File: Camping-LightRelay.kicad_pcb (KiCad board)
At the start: 2 copper layers, 58 x 63 mm, 91 parts, among them CN1 U262-061N-4BVC11, CN101 XHP-2, CN2 907-152A1022D10200, CN3 907-152A1022D10200, CN4 B2B-XH-A, Q1 FDV301N, Q2 BC817, Q3 IRF7404, Q4 BSS138, U1 USBLC6-2SC6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

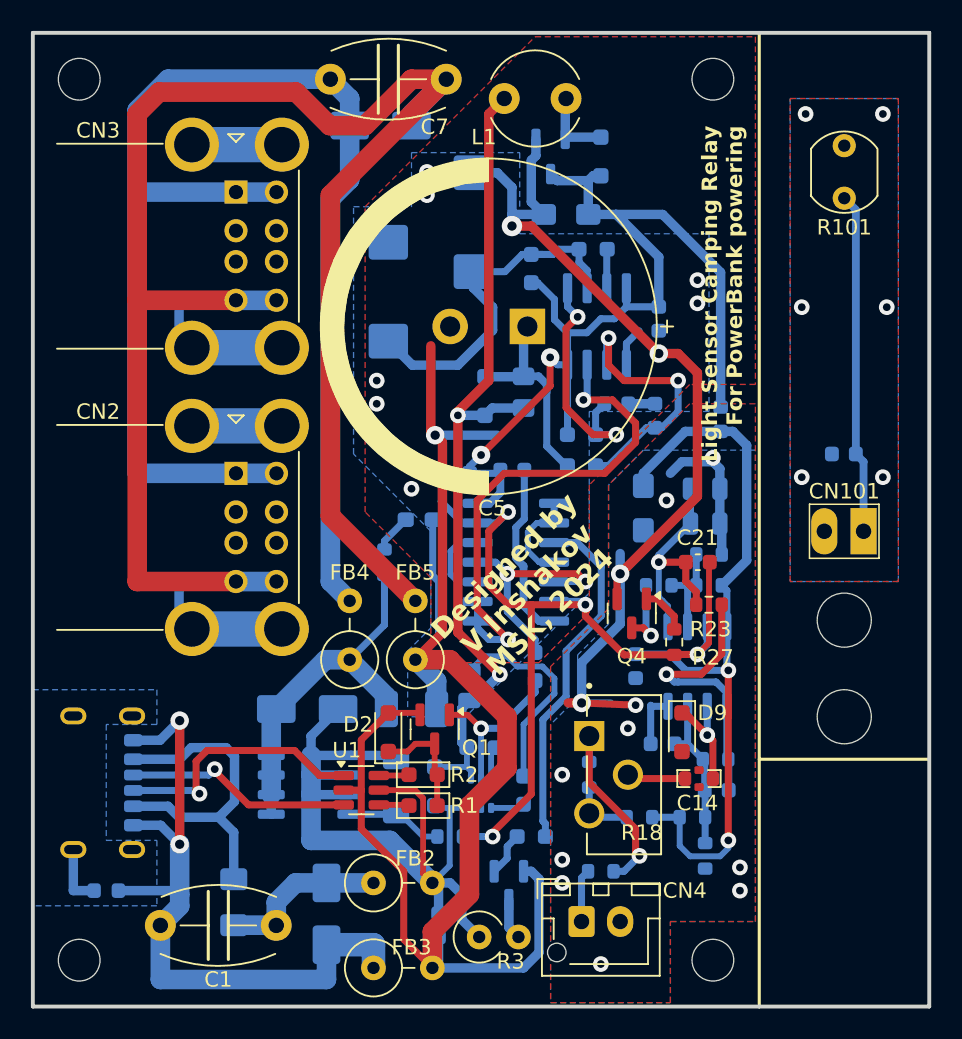
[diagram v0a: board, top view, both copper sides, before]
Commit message: Мелкий рефакторинг
- Обновление Readme.md
- Правки в печатную плату
- Переименование сигналов
- добавление исключений в .gitignore
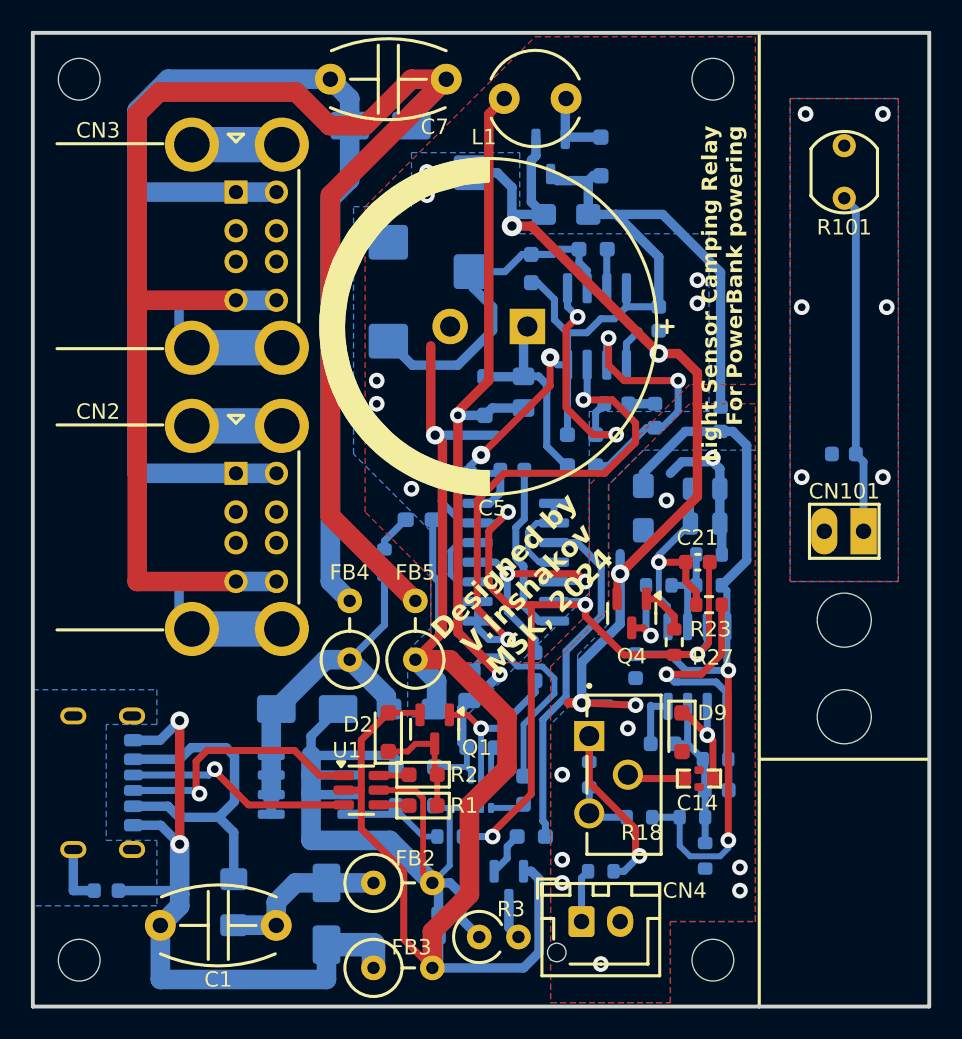
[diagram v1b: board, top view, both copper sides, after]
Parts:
- C20: value 10uF -> 22uF
- C4: value 100uFx10V -> 10uFx16V; footprint Capacitor_Tantalum_SMD:CP_EIA-3528-15_AVX-H_Pad1.50x2.35mm_HandSolder -> Capacitor_Tantalum_SMD:CP_EIA-3216-12_Kemet-S_Pad1.58x1.35mm_HandSolder
- D3: value BAT20J -> 1N4148WS
- D4: value BZV55C6V8 -> SD05C; footprint Diode_SMD:D_MiniMELF -> Diode_SMD:D_SOD-323_HandSoldering
- R1, R2: value 5.1k 1% -> 5.1k
- R10: value 470 -> 560
- R17: value 180k 1% -> 180k
- R19: value 10k 1% -> 10k
- R20: value 82k 1% -> 82k
- R21: value 100k 1% -> 100k
- R3: value 43 -> 47 1W; footprint Resistor_THT:R_Axial_DIN0309_L9.0mm_D3.2mm_P2.54mm_Vertical -> PCM_Resistor_THT_AKL:R_Axial_DIN0309_L9.0mm_D3.2mm_P2.54mm_Vertical
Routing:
- net (no net): track 0.00 -> 11.6 mm
- net Net-(CN3-Shield): track 16.6 -> 10.8 mm
- net Net-(CN2-Shield): track 15.1 -> 9.23 mm
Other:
- board text added: "Скайбирование"
